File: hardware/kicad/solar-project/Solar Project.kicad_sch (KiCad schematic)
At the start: 2 parts

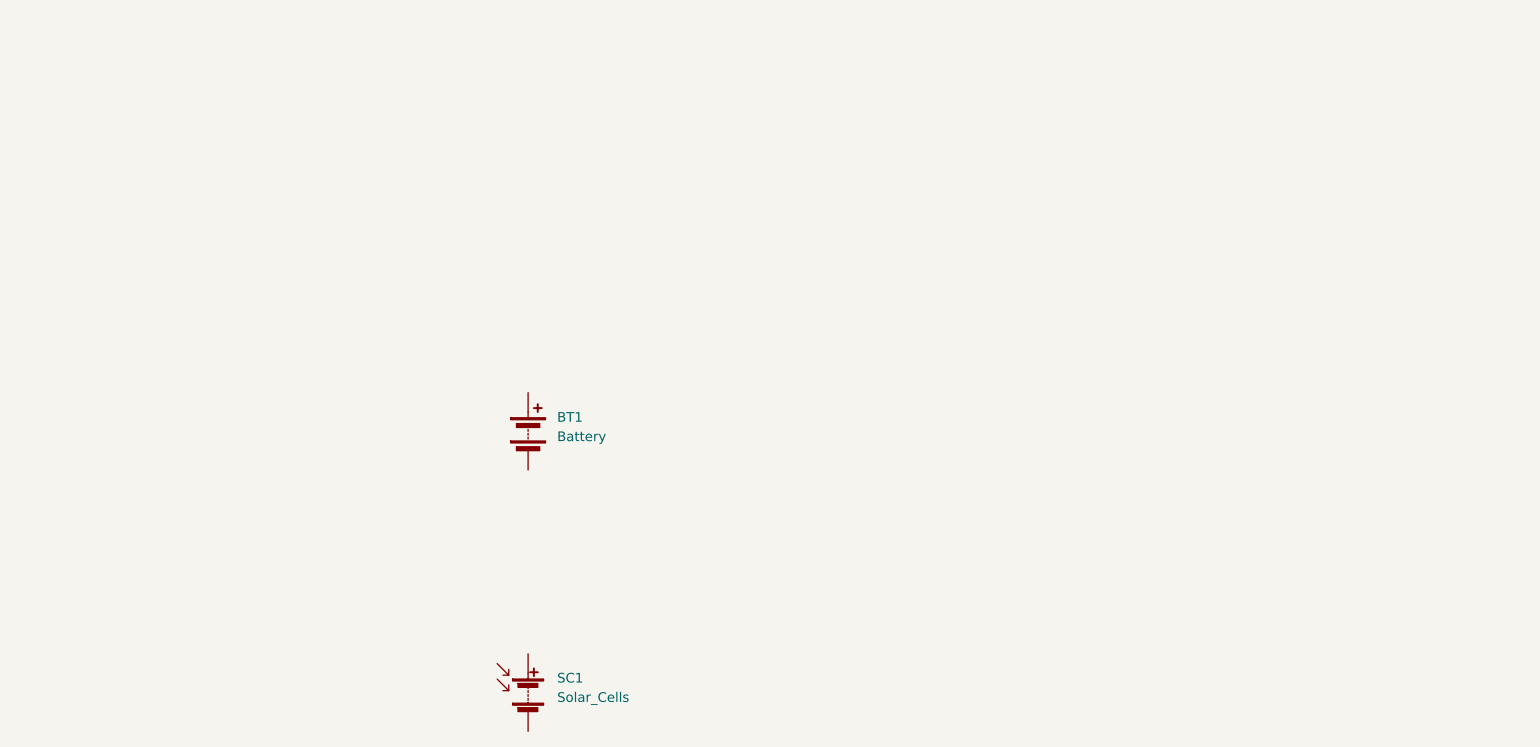
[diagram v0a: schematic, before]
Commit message: Consolidate KiCad source path and log migration state
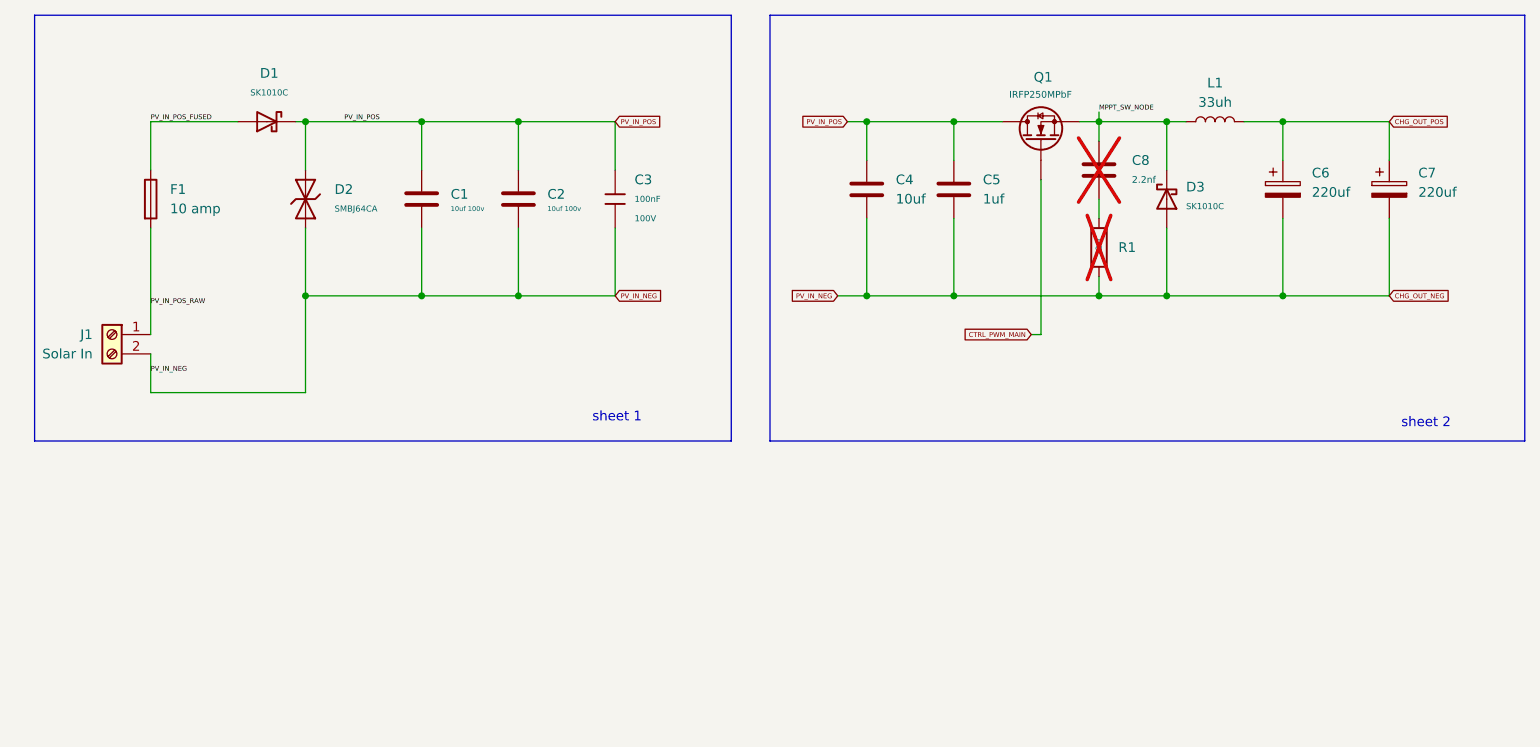
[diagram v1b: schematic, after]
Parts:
- removed BT1: Battery, symbol Device:Battery
- removed SC1: Solar_Cells, symbol Device:Solar_Cells
- added C1, C2: 10uf 100v, Capacitor_SMD:C_1210_3225Metric, symbol Device:C
- added C3: 100nF, PCM_JLCPCB:C_0805, symbol PCM_JLCPCB-Capacitors:0805,100nF
- added C4: 10uf, SMD,D6.3xL7.7mm, symbol Device:C
- added C5: 1uf, Capacitor_SMD:C_1206_3216Metric, symbol Device:C
- added C6, C7: 220uf, Through Hole,D6.3xL9mm, symbol Device:C_Polarized
- added C8: 2.2nf, symbol Device:C
- added D1, D3: SK1010C, PCM_JLCPCB:D_SMC, symbol PCM_JLCPCB-Diodes_1:Schottky,SK1010C
- added D2: SMBJ64CA, PCM_JLCPCB:D_SMB, symbol PCM_JLCPCB-Diodes_1:TVS-Bi,SMBJ64CA
- added F1: 10 amp, symbol Device:Fuse
- added J1: Solar In, symbol Connector:Screw_Terminal_01x02
- added L1: 33uh, symbol Device:L
- added Q1: IRFP250MPbF, Package_TO_SOT_THT:TO-247-3_Vertical, symbol Device:Q_NMOS
- added R1: 22Ω, PCM_JLCPCB:R_1206, symbol PCM_JLCPCB-Resistors:1206,22Ω
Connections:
- new net: C8.2, R1.1
- new net CHG_OUT_NEG: C1.2, C2.2, C3.2, C4.2, C5.2, C6.2, C7.2, D2.1, D3.2, J1.2 (Pin_2), R1.2
- new net CHG_OUT_POS: C6.1, C7.1, L1.2
- new net CTRL_PWM_MAIN: Q1.G
- new net MPPT_SW_NODE: C8.1, D3.1, L1.1, Q1.S
- new net PV_IN_POS: C1.1, C2.1, C3.1, C4.1, C5.1, D1.1, D2.2, Q1.D
- new net PV_IN_POS_FUSED: D1.2, F1.1
- new net PV_IN_POS_RAW: F1.2, J1.1 (Pin_1)
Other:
- note added: "sheet 1"
- note added: "sheet 2"

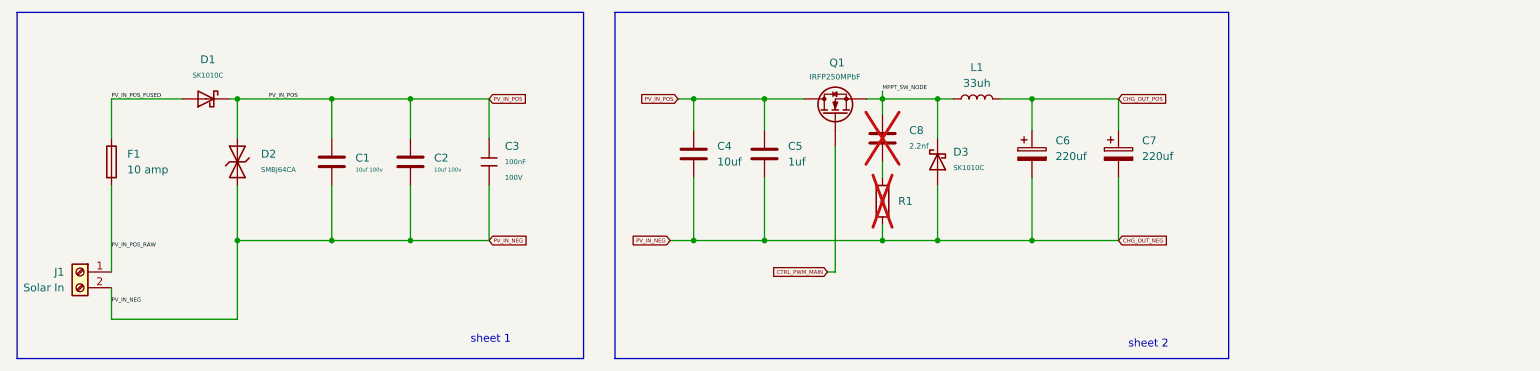
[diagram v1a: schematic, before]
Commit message: Temporarily clear Q1 gate ERC blocker for Rev0 progress
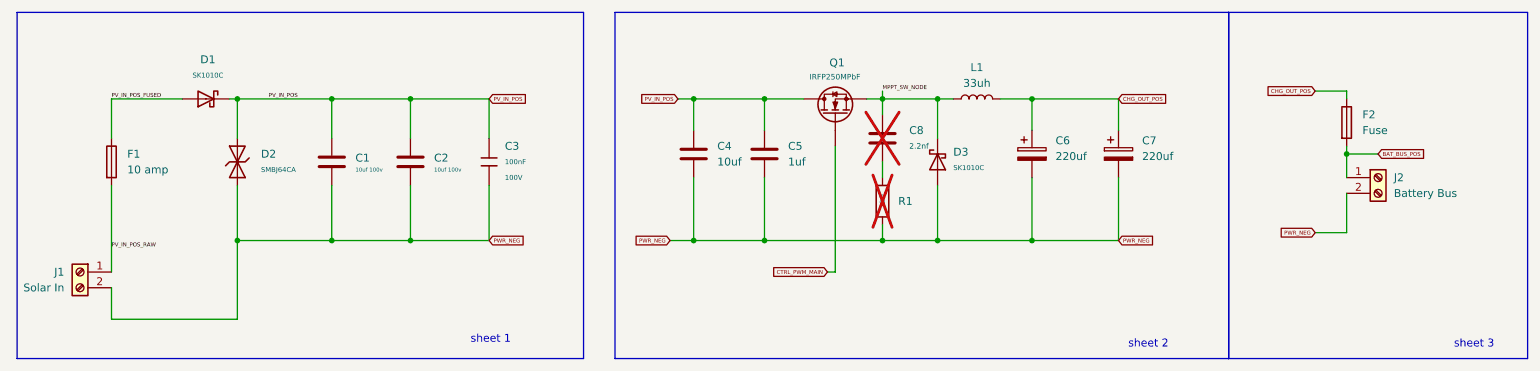
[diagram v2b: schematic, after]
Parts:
- added F2: Fuse, symbol Device:Fuse
- added J2: Battery Bus, symbol Connector:Screw_Terminal_01x02
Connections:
- net CHG_OUT_POS: now also F2.1
- net CHG_OUT_NEG renamed PWR_NEG
- net PWR_NEG: now also J2.2 (Pin_2)
- new net BAT_BUS_POS: F2.2, J2.1 (Pin_1)
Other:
- note added: "sheet 3"

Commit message: Zone D Phase 1 complete: Add sensing and control I/O placeholders with measurement circuits, thermal sensors, and control net boundaries
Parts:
- added J3: (J_LOG), symbol Connector:Conn_01x03_Pin
- added J4: U_CTRL, symbol Connector:Conn_01x12_Pin
- added R2, R27: 10kΩ, PCM_JLCPCB:R_0805, symbol PCM_JLCPCB-Resistors:0805,10kΩ
- added R28, R3: 1kΩ, PCM_JLCPCB:R_0805, symbol PCM_JLCPCB-Resistors:0805,1kΩ
- added TH1, TH2: Thermistor_NTC, symbol Device:Thermistor_NTC
- added TP_BAT_I, TP_BAT_V, TP_PV_I, TP_PV_V: TestPoint, symbol Connector:TestPoint
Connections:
- net BAT_BUS_POS: now also J4.6 (Pin_6), R2.1, TP_BAT_I.1
- net CHG_OUT_POS: now also J4.4 (Pin_4), TP_PV_I.1
- net CTRL_PWM_MAIN: now also J4.1 (Pin_1)
- net PV_IN_POS: now also R27.1
- net PWR_NEG: now also J3.3 (Pin_3), R28.2, R3.2, TH1.2, TH2.2
- new net CTRL_EN_CHG: J4.2 (Pin_2)
- new net FAULT_OCP: J4.10 (Pin_10)
- new net FAULT_OVP: J4.9 (Pin_9)
- new net SENSE_BAT_V: J4.5 (Pin_5), R2.2, R3.1, TP_BAT_V.1
- new net SENSE_PV_V: J4.3 (Pin_3), R27.2, R28.1, TP_PV_V.1
- new net SENSE_TEMP_BOARD: J4.8 (Pin_8), TH2.1
- new net SENSE_TEMP_PWR: J4.7 (Pin_7), TH1.1
- new net UART_RX_CFG : J3.2 (Pin_2), J4.12 (Pin_12)
- new net UART_TX_LOG: J3.1 (Pin_1), J4.11 (Pin_11)
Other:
- note added: "Battery Current"
- note added: "Battery voltage"
- note added: "Header (J_LOG)"
- note added: "Over-Current Protection (FAULT_OCP)"
- note added: "Over-Voltage Protection (FAULT_OVP)"
- note added: "PV Current"
- note added: "PV voltage"
- note added: "TH_Board"
- note added: "TH_PWR"
- note added: "U_CTRL"
- note added: "Zone B"
- note added: "Zone C"
- note added: "Zone D"
- note added: "zone A"
- note removed: "sheet 1"
- note removed: "sheet 2"
- note removed: "sheet 3"

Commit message: schematic/docs: LM51772 U6 miswire cleanup, ERC 14->7 errors
- Fix U6 RST/SYNC/DTRK/VCC2/FLT miswires; apply Rev 0 straps
  - RST (pin 38) -> CTRL_3V3 (pull-high, normal operation)
  - SYNC (pin 3) -> PWR_NEG (free-running oscillator, Rev 0 strap)
  - DTRK (pin 4) -> PWR_NEG (tracking disabled, Rev 0 strap)
  - VCC2 (pin 29) -> U6_VCC2 placeholder (output, decoupling needed)
  - FLT (pin 11) -> U6_FLT placeholder (pull-up needed)
- VIN/BIAS: both pins on PV_IN_POS intentional for Rev 0 simplicity
- Normalize net labels: UART_RX_CFG, V_in_ADC (remove split-risk spaces)
- Fix gate-drive pin_not_driven (M1-M4): change U6 HO1/LO1/HO2/LO2
  from unspecified to output type in embedded lib_symbols
- Fix R32 pin 2 floating: add PWR_NEG label at (93.98, 219.71)
- ERC: 14 errors -> 7 errors; all remaining are deferred power-authority
  semantics (VIN/PGND/VBAT/U4-VIN no PWR_FLAG, D3 library type)
- Add SOLAR_HANDOFF_2026-07-19.md and update NEXT_CHAT_PROMPT.md
- Add LM51772/LM851772 datasheets and WEBENCH PDFs to docs/
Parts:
- removed C1, C2: 10uf 100v, Capacitor_SMD:C_1210_3225Metric, symbol Device:C
- removed C3: 100nF, PCM_JLCPCB:C_0805, symbol PCM_JLCPCB-Capacitors:0805,100nF
- removed C6, C7: 220uf, Through Hole,D6.3xL9mm, symbol Device:C_Polarized
- removed C8: 2.2nf, symbol Device:C
- removed D1, D3: SK1010C, PCM_JLCPCB:D_SMC, symbol PCM_JLCPCB-Diodes_1:Schottky,SK1010C
- removed J4: U_CTRL, symbol Connector:Conn_01x12_Pin
- removed L1: 33uh, symbol Device:L
- removed Q1: IRFP250MPbF, Package_TO_SOT_THT:TO-247-3_Vertical, symbol Device:Q_NMOS
- removed R1: 22Ω, PCM_JLCPCB:R_1206, symbol PCM_JLCPCB-Resistors:1206,22Ω
- removed R2, R27: 10kΩ, PCM_JLCPCB:R_0805, symbol PCM_JLCPCB-Resistors:0805,10kΩ
- removed R28, R3: 1kΩ, PCM_JLCPCB:R_0805, symbol PCM_JLCPCB-Resistors:0805,1kΩ
- removed TP_BAT_I, TP_BAT_V, TP_PV_I, TP_PV_V: TestPoint, symbol Connector:TestPoint
- added C1, C12, C22: 100nF, PCM_JLCPCB:C_0805, symbol PCM_JLCPCB-Capacitors:0805,100nF
- added C10: 47pF, PCM_JLCPCB:C_0805, symbol PCM_JLCPCB-Capacitors:0805,47pF
- added C11, C15, C33, C34, C35, C7, C8: 2.2uF, PCM_JLCPCB:C_1206, symbol PCM_JLCPCB-Capacitors_1:1206,2.2uF
- added C13, C9: 2.2nF, PCM_JLCPCB:C_0805, symbol PCM_JLCPCB-Capacitors:0805,2.2nF
- added C14: 100uF, PCM_JLCPCB:C_1206, symbol PCM_JLCPCB-Capacitors:1206,100uF
- added C16: 10uf, SMD,D6.3xL7.7mm, symbol Device:C
- added C17, C19, C3, C30, C31, C32, C36, C37, C38, C39, C40, C41, C42, C43, C6: 47uf, Capacitor_THT:CP_Radial_D6.3mm_P2.50mm, symbol Device:C
- added C18, C21: 560uf, SMD,D10xL12.6mm, symbol Device:C
- added C2: 1uF, PCM_JLCPCB:C_0805, symbol PCM_JLCPCB-Capacitors:0805,1uF
- added C20: 180pf, PCM_JLCPCB:C_0805, symbol Device:C
- added C23, C28: 100nf, PCM_JLCPCB:C_0805, symbol Device:C
- added C24: 220nf, PCM_JLCPCB:C_0805, symbol Device:C
- added C25: 1.5nf, PCM_JLCPCB:C_0805, symbol Device:C
- added C26: 33nf, PCM_JLCPCB:C_0805, symbol Device:C
- added C27, C29: 22uF, PCM_JLCPCB:C_0805, symbol PCM_JLCPCB-Capacitors:0805,22uF
- added D1, D5: 1SMA4742A, PCM_JLCPCB:D_DO-214AC(SMA), symbol PCM_JLCPCB-Diodes:Zener,1SMA4742A
- added D3: USBLC6-2SC6, digikey-footprints:SOT23-6L, symbol dk_TVS-Diodes:USBLC6-2SC6
- added D4: 1N5819WS, PCM_JLCPCB:D_SOD-323, symbol PCM_JLCPCB-Diodes:Schottky,1N5819WS
- added J5: Connector,_USB-TYPE-C-16P, symbol 1My_parts - Connectors:Connector,_USB-TYPE-C-16P
- added L2: 1uh, symbol Device:L
- added L3: 68uh, SMD,7.1x6.6mm, symbol Device:L
- added M1: IPZ40N, TSDSON-8FL, symbol Device:Q_NMOS
- added M2, M3, M4: Q_NMOS, symbol Device:Q_NMOS
- added Q1, Q2: BSS138, PCM_JLCPCB:Q_SOT-23, symbol PCM_JLCPCB-Transistors:NMOS,BSS138
- added R1, R4: 5.1kΩ, PCM_JLCPCB:R_0805, symbol PCM_JLCPCB-Resistors:0805,5.1kΩ
- added R10, R6: 22kΩ, PCM_JLCPCB:R_0805, symbol PCM_JLCPCB-Resistors:0805,22kΩ
- added R11: 240k, PCM_JLCPCB:R_0805, symbol Device:R
- added R12: 6.8kΩ, PCM_JLCPCB:R_0805, symbol PCM_JLCPCB-Resistors:0805,6.8kΩ
- added R13: 1MΩ, PCM_JLCPCB:R_0805, symbol PCM_JLCPCB-Resistors:0805,1MΩ
- added R14: 330kΩ, PCM_JLCPCB:R_0805, symbol PCM_JLCPCB-Resistors_1:0805,330kΩ
- added R15: 2kΩ, PCM_JLCPCB:R_0805, symbol PCM_JLCPCB-Resistors_1:0805,2kΩ
- added R16, R22: 0.001ohms, symbol Device:R_Shunt
- added R17, R25: 5.62k, symbol Device:R
- added R18: 66.5k, symbol Device:R
- added R19, R21, R26, R27, R34, R39, R41, R42: 10Ω, PCM_JLCPCB:R_0805, symbol PCM_JLCPCB-Resistors:0805,10Ω
- added R20: 0.010, 2818, symbol Device:R
- added R23: 75k, symbol Device:R
- added R24: 21.5k, digikey-footprints:0805, symbol Device:R
- added R28: 51.7k, symbol Device:R
- added R29: 20.5k, symbol Device:R
- added R3: 66.5k, digikey-footprints:0805, symbol Device:R
- added R30: 40.2k, symbol Device:R
- added R31: 2.43K, symbol Device:R
- added R32, R37, R38, R40, R43: 100kΩ, PCM_JLCPCB:R_0805, symbol PCM_JLCPCB-Resistors:0805,100kΩ
- added R33: 6.49k, symbol Device:R
- added R35: 180kΩ, PCM_JLCPCB:R_0805, symbol PCM_JLCPCB-Resistors:0805,180kΩ
- added R36: 10kΩ, PCM_JLCPCB:R_0805, symbol PCM_JLCPCB-Resistors_1:0805,10kΩ
- added R5: 4.7kΩ, PCM_JLCPCB:R_0805, symbol PCM_JLCPCB-Resistors:0805,4.7kΩ
- added R7: 430k, PCM_JLCPCB:R_0805, symbol PCM_JLCPCB-Resistors:0805,49.9kΩ
- added R8: 27kΩ, PCM_JLCPCB:R_0805, symbol PCM_JLCPCB-Resistors:0805,27kΩ
- added R9: 180k, PCM_JLCPCB:R_0805, symbol Device:R
- added U1: STM32G431CBU6, STM32G431CBU6:QFN50P700X700X60-49N, symbol 1My_MPUs:STM32G431CBU6
- added U2: BSC112N06LD, Package_SON:Infineon_PG-TDSON-8_6.15x5.15mm, symbol 1My_Basic components:BSC112N06LD
- added U3: CP2102-GMR, PCM_JLCPCB:WQFN-28_L5.0-W5.0-P0.50-BL-EP3.2, symbol PCM_JLCPCB-Interface:Transceiver, USB
- added U4: LM5163DDAR, Package_SO:Texas_R-ESOP-8, symbol 1My_IC's:LM5163
- added U5: BSC155N06ND, Package_SON:Infineon_PG-TDSON-8_6.15x5.15mm, symbol 1My_Basic components:BSC155N06ND
- added U6: LM51772QRHARQ1, Package_DFN_QFN:Texas_RHA0040B_VQFN-40-1EP_6x6mm_P0.5mm_EP4.15x4.15mm, symbol 1My_IC's:LM51772QRHARQ1
- C4: value 10uf -> 47uf; footprint SMD,D6.3xL7.7mm -> Capacitor_THT:CP_Radial_D6.3mm_P2.50mm; LCSC C72482 -> C122243
- C5: value 1uf -> 47uf; footprint Capacitor_SMD:C_1206_3216Metric -> Capacitor_THT:CP_Radial_D6.3mm_P2.50mm; LCSC C91151 -> C122243
- F1: footprint (none) -> Fuse:Fuseholder_Littelfuse_100_series_5x25mm; LCSC (none) -> C142864
- renumbered J3 to J2, J2 to J3
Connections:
- net BAT_BUS_POS: now also D4.2, R20.1, R21.1; no longer J3.1 (Pin_1)
- net CHG_OUT_POS: now also U5.7 (D2), U5.8 (D2), U6.18 (VOUT)
- net CTRL_EN_CHG: now also U1.43 (PB5)
- net FAULT_OCP: now also U1.17 (PB0)
- net FAULT_OVP: now also U1.18 (PB1)
- net PV_IN_POS: now also C11.2, C16.1, C19.1, C28.1, C32.1, C36.1, C37.1, C38.2, C39.2, C40.2, C41.2, C42.1, C43.2, C7.1, C8.2, M1.D, R18.1, R23.1, U2.7 (D2), U2.8 (D2), U6.36 (VIN), U6.40 (BIAS); no longer C4.1, C5.1, D2.2
- net PV_IN_POS_FUSED: now also D2.2, R35.1, R43.1, U2.5 (D1), U2.6 (D1)
- net PWR_NEG: now also C4.1, C1.2, C11.1, C12.2, C14.2, C15.2, C16.2, C17.2, C18.2, C19.2, C2.2, C21.2, C28.2, C29.2, C3.2, C30.1, C31.1, C32.2, C33.2, C34.1, C35.1, C36.2, C37.2, C38.1, C39.1, C40.1, C41.1, C42.2, C43.1, C6.1, C7.2, C8.1, D3.2, J5.A12B1 (GND), J5.B12A1 (GND), J5.S1 (SHIELD), M2.S, M3.S, Q1.2 (S), Q2.2 (S), R1.1, R11.1, R15.2, R17.2, R24.2, R25.2, R32.2, R36.2, R4.1, R8.2, U1.49 (VSS), U3.3 (GND), U4.1 (GND), U6.17 (AGND), U6.3 (SYNC), U6.4 (DTRK), U6.41 (GND); no longer C4.2
- net SENSE_TEMP_BOARD: now also U1.15 (PA7)
- net SENSE_TEMP_PWR: now also U1.14 (PA6)
- net UART_RX_CFG  renamed UART_RX_CFG
- new net: C10.1, C9.2, R12.2
- new net: C10.2, R6.2, R7.1, U4.5 (FB)
- new net: Q1.1 (G), R37.2, R39.2
- new net: R14.2, R15.1
- new net: D5.2, U5.1 (S1), U5.3 (S2)
- new net: D5.1, R34.2, U5.2 (G1), U5.4 (G2)
- new net: R16.1, R38.1, U5.5 (D1), U5.6 (D1)
- new net: Q2.3 (D), R42.1, R43.2
- new net: D1.1, R42.2, U2.2 (G1), U2.4 (G2)
- new net: R11.2, R6.1
- new net: C15.1, D4.1, R13.1, U4.2 (VIN)
- new net: Q1.3 (D), R34.1, R38.2
- new net: R30.1, U6.10 (CDC)
- new net: R5.1, U3.9 (RST#)
- new net: R33.1, U6.9 (ADDR_SLOPE_CFG1)
- new net: Q2.1 (G), R40.2, R41.2
- new net: R28.1, U6.12 (RT)
- new net: D1.2, U2.1 (S1), U2.3 (S2)
- new net: C22.1, U6.25 (HB1)
- new net: D3.1, J5.A7 (D-), J5.B7 (D-)
- new net: D3.3, J5.A6 (D+), J5.B6 (D+)
- new net: D3.4, U3.4 (D+)
- new net: D3.6, U3.5 (D-)
- new net: C13.1, L3.1, R9.2, U4.8 (SW)
- new net: C13.2, U4.7 (BST)
- new net: R13.2, R14.1, U4.3 (EN/UVLO)
- new net: R8.1, U4.4 (RON)
- new net: C23.1, U6.31 (HB2)
- new net: C29.1, R32.1, U6.16 (ILIMCOMP_ISET), U6.7 (MODE)
- new net: R12.1, R9.1
- new net: C27.1, U6.1 (VCC1)
- new net: C26.2, U6.2 (SS_ATRK)
- new net: C20.2, R27.2, U6.21 (CSB)
- new net: C20.1, R26.2, U6.22 (CSA)
- new net: R29.1, U6.8 (CFG2)
- new net: C24.2, C25.2, U6.13 (COMP)
- new net: L2.1, R22.1
- new net: C24.1, R31.1
- new net: J3.1 (Pin_1), R19.1, R20.2
- new net: J5.A5 (CC1), R1.2
- new net: R10.1, R7.2
- new net: J5.A8 (SBU1), J5.B8 (SBU2)
- new net: J5.B5 (CC2), R4.2
- new net BAT_I_NEG: R19.2
- new net BAT_I_POS: R21.2
- new net CTS: U3.23 (CTS)
- new net DRV1: U6.35 (DRV1)
- new net HO1: M1.G, U6.24 (HO1)
- new net HO2: M4.G, U6.32 (HO2)
- new net I2C CLK: U1.45 (PB7), U6.6 (SCL_CFG4)
- new net I2C DATA: U1.44 (PB6), U6.5 (SDA_CFG3)
- new net ISNSN: R16.2, U6.19 (ISNSN)
- new net ISNSP: R16.3, U6.20 (ISNSP)
- new net LO1: M2.G, U6.27 (LO1)
- new net LO2: M3.G, U6.30 (LO2)
- new net PGND: C25.1, C26.1, C27.2, R28.2, R29.2, R30.2, R31.2, R33.2, U6.28 (PGND)
- new net RTS: U3.24 (RTS)
- new net RXD: U1.31 (PA9), U3.25 (RXD)
- new net SWCLK: U1.37 (PA14)
- new net SWDIO: U1.36 (PA13)
- new net SW_1: C22.2, M1.S, M2.D, R22.4, U6.23 (SW1)
- new net SW_2: C23.2, L2.2, M3.D, M4.S, U6.33 (SW2)
- new net TXD: U1.32 (PA10), U3.26 (TXD)
- new net U6_FLT: U6.11 (FLT)
- new net U6_VCC2: U6.29 (VCC2)
- new net VBUS: C1.1, C2.1, D3.5, J5.A9B4 (VBUS), J5.B9A4 (VBUS), U3.7 (REGIN), U3.8 (VBUS)
- new net VDD: C12.1, C14.1, C9.1, L3.2, R10.2, R37.1, R40.1, R5.2, U1.1 (VBAT), U1.20 (VREF+), U1.21 (VDDA), U1.23 (VDD), U1.35 (VDD), U1.48 (VDD), U3.6 (VDD), U6.38 (RST)
- new net V_in_ADC: R35.2, R36.1, U1.12 (PA4)
- new net V_in_FB: R17.1, R18.2, U6.15 (VIN-FB)
- new net V_in_ON: R41.1, U1.13 (PA5)
- new net V_out: C17.1, C18.1, C21.1, C3.1, C30.2, C31.2, C33.1, C34.2, C35.2, C4.2, C5.1, C6.2, M4.D, R16.4, R3.1
- new net V_out _on: R39.1, U1.30 (PA8)
- new net _CSA_2: R22.3, R26.1
- new net _CSB_2: R22.2, R27.1
- new net _OUTPUT Feedback: R25.1, R3.2, U6.14 (FB_INT)
- new net _Undervoltage Feedback: R23.2, R24.1, U6.37 (EN_UVLO)
- no-connect marks 0 -> 50
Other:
- note added: "Cout"
- note added: "Disconnect"
- note added: "Input Caps"
- note added: "Output Caps"
- note removed: "U_CTRL"
- note removed: "Zone B"
- moved on the sheet: F1, F2, J1, J2, J3, TH1, TH2

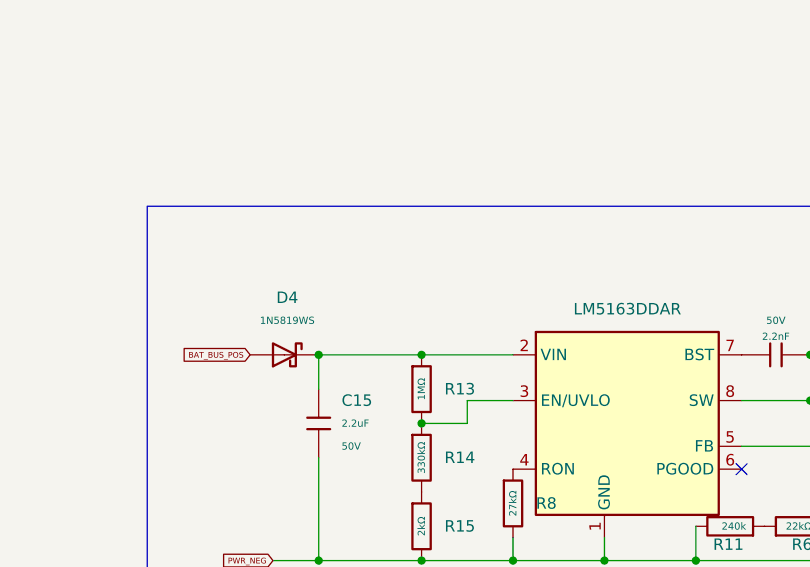
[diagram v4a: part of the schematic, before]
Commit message: schematic: wire CTRL_SUPPLY_IN - add D6/D7 OR-ing diodes, name net
DEC-013 gap closed: U4 VIN was an unnamed auto-net with only BAT path.
- Add D6 (1N5819WS): CHG_OUT_POS anode at (294.64,182.88) -> cathode at CTRL_SUPPLY_IN
- Add D7 (1N5819WS): VBUS anode at (294.64,177.80) -> cathode at CTRL_SUPPLY_IN
- Add 3 connecting wires joining D6/D7 cathodes to bus junction at (309.88,187.96)
- Add CTRL_SUPPLY_IN global label at (320.04,187.96) naming the previously
  anonymous Net-(U4-VIN) as the documented CTRL_SUPPLY_IN boundary net
- D4 (BAT_BUS_POS) already present; all three source paths now OR into CTRL_SUPPLY_IN
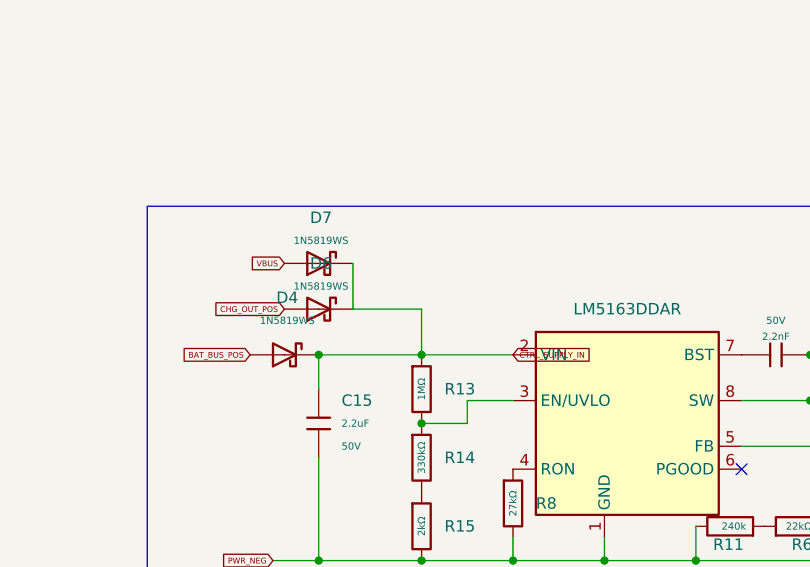
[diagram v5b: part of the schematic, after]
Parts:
- added D6, D7: 1N5819WS, PCM_JLCPCB:D_SOD-323, symbol PCM_JLCPCB-Diodes:Schottky,1N5819WS
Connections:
- net CHG_OUT_POS: now also D6.2
- net VBUS: now also D7.2
- net CTRL_SUPPLY_IN: now reaches C15.1, D4.1, R13.1, U4.2 (VIN)
- net CTRL_SUPPLY_IN: now also D6.1, D7.1

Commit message: cleanup: revert C30/R34 temp components - maintain clean CTRL_SUPPLY_IN OR-ing wiring
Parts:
- removed C30: 47uf, Capacitor_THT:CP_Radial_D6.3mm_P2.50mm, symbol Device:C
- removed R34: 10Ω, PCM_JLCPCB:R_0805, symbol PCM_JLCPCB-Resistors:0805,10Ω
